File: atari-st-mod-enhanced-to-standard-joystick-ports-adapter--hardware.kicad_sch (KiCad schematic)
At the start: 45 parts, among them J1 Joy0/Mouse, J2 Joy1, J3 OLED 128×64, J4 Enhanced Joystick Port, J5 Joy0/Mouse, J6 Joy1, Q1 1<Vgsth<2, Low Rdson, Vds >10, Q10 1<Vgsth<2, Low Rdson, Vds >10, Q2 1<Vgsth<2, Low Rdson, Vds >10, Q3 1<Vgsth<2, Low Rdson, Vds >10, Q4 1<Vgsth<2, Low Rdson, Vds >10, Q5 1<Vgsth<2, Low Rdson, Vds >10, Q6 1<Vgsth<2, Low Rdson, Vds >10, Q7 1<Vgsth<2, Low Rdson, Vds >10, Q8 1<Vgsth<2, Low Rdson, Vds >10, Q9 1<Vgsth<2, Low Rdson, Vds >10, SW1 Reset, SW2 Selector, SW3 Activate/Change, SW4 Cancel, U1 LM4040DBZ-3

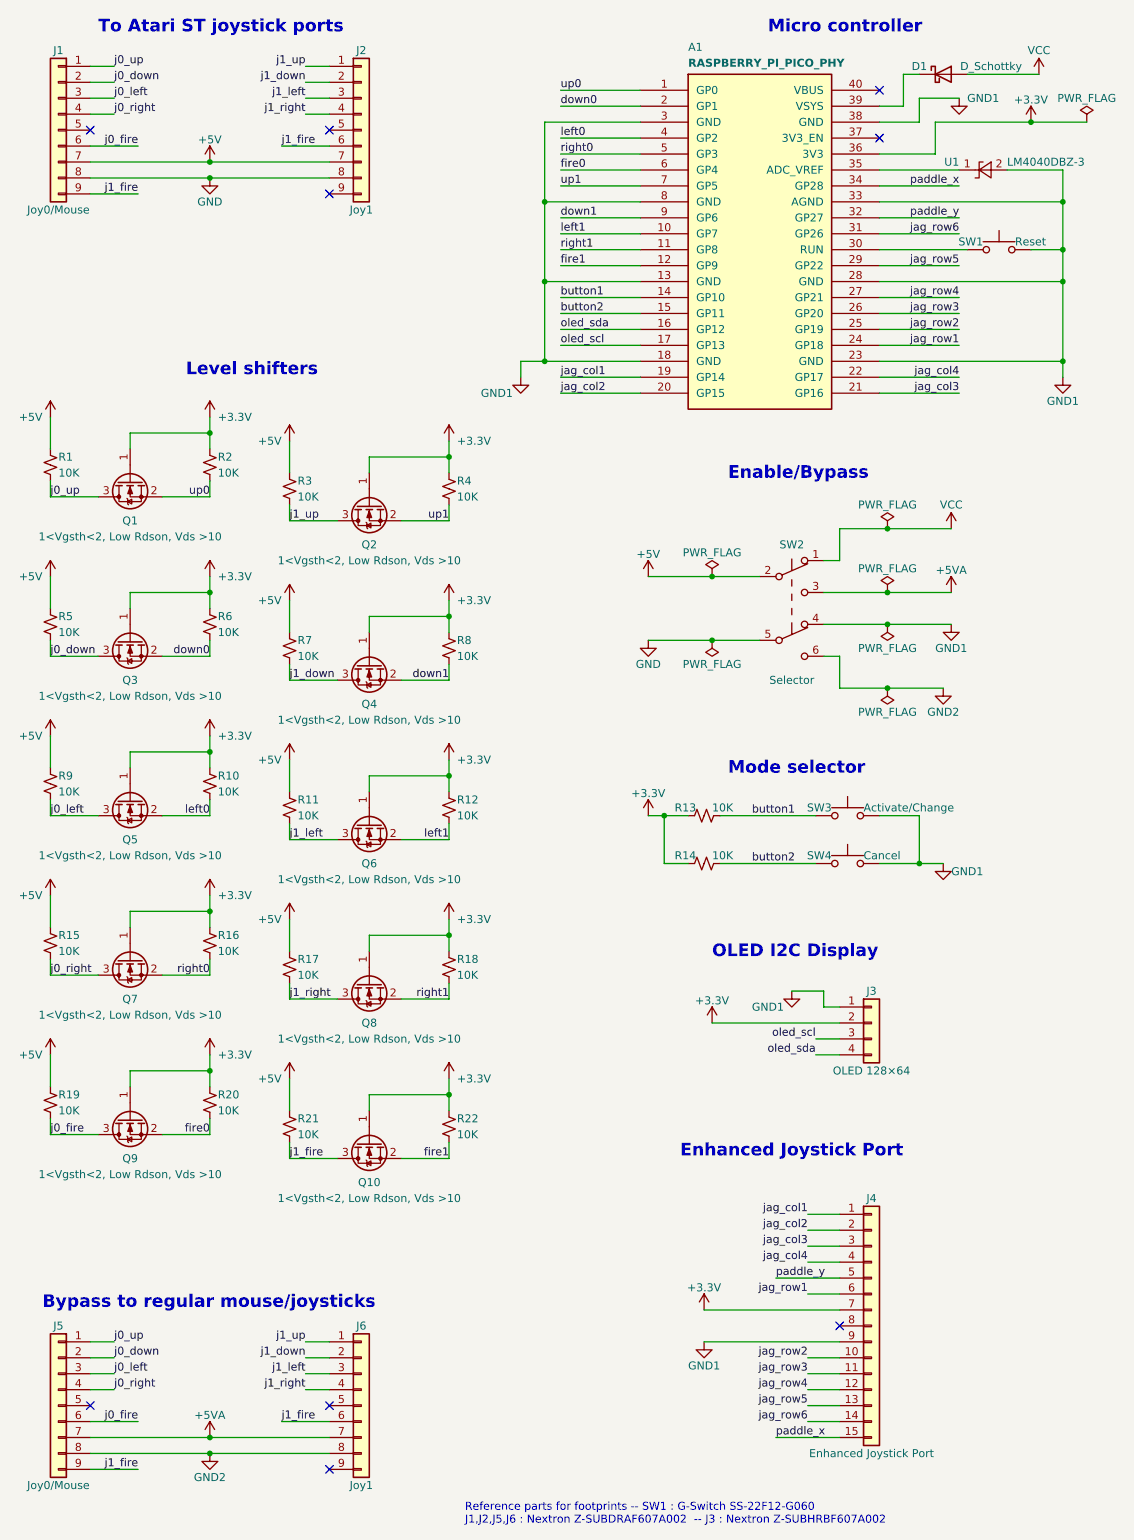
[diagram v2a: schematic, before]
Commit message: rearrange connexion for easier routing
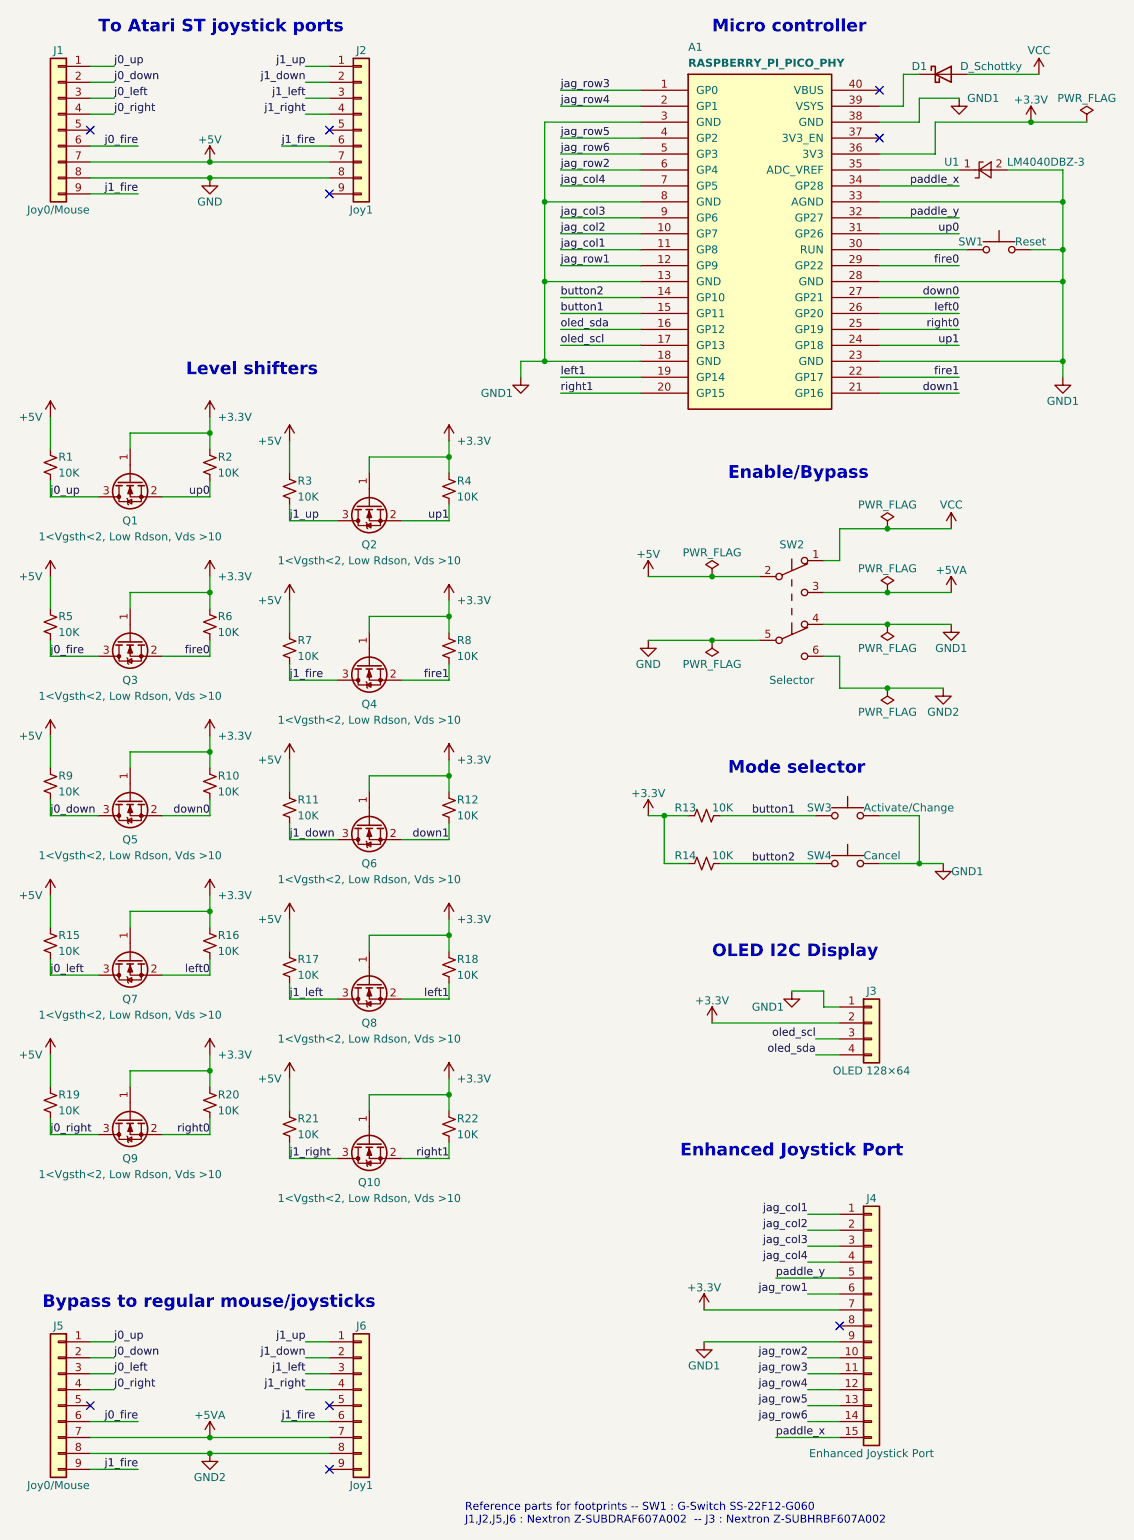
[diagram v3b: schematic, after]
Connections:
- net button1: now also A1.15 (GP11); no longer A1.14 (GP10)
- net button2: now also A1.14 (GP10); no longer A1.15 (GP11)
- net down0: now also A1.27 (GP21), Q5.2 (S), R10.2; no longer A1.2 (GP1), Q3.2 (S), R6.2
- net down1: now also A1.21 (GP16), Q6.2 (S), R12.2; no longer A1.9 (GP6), Q4.2 (S), R8.2
- net fire0: now also A1.29 (GP22), Q3.2 (S), R6.2; no longer A1.6 (GP4), Q9.2 (S), R20.2
- net fire1: now also A1.22 (GP17), Q4.2 (S), R8.2; no longer A1.12 (GP9), Q10.2 (S), R22.2
- net j0_down: now also Q5.3 (D), R9.2; no longer Q3.3 (D), R5.2
- net j0_fire: now also Q3.3 (D), R5.2; no longer Q9.3 (D), R19.2
- net j0_left: now also Q7.3 (D), R15.2; no longer Q5.3 (D), R9.2
- net j0_right: now also Q9.3 (D), R19.2; no longer Q7.3 (D), R15.2
- net j1_down: now also Q6.3 (D), R11.2; no longer Q4.3 (D), R7.2
- net j1_fire: now also Q4.3 (D), R7.2; no longer Q10.3 (D), R21.2
- net j1_left: now also Q8.3 (D), R17.2; no longer Q6.3 (D), R11.2
- net j1_right: now also Q10.3 (D), R21.2; no longer Q8.3 (D), R17.2
- net jag_col1: now also A1.11 (GP8); no longer A1.19 (GP14)
- net jag_col2: now also A1.10 (GP7); no longer A1.20 (GP15)
- net jag_col3: now also A1.9 (GP6); no longer A1.21 (GP16)
- net jag_col4: now also A1.7 (GP5); no longer A1.22 (GP17)
- net jag_row1: now also A1.12 (GP9); no longer A1.24 (GP18)
- net jag_row2: now also A1.6 (GP4); no longer A1.25 (GP19)
- net jag_row3: now also A1.1 (GP0); no longer A1.26 (GP20)
- net jag_row4: now also A1.2 (GP1); no longer A1.27 (GP21)
- net jag_row5: now also A1.4 (GP2); no longer A1.29 (GP22)
- net jag_row6: now also A1.5 (GP3); no longer A1.31 (GP26)
- net left0: now also A1.26 (GP20), Q7.2 (S), R16.2; no longer A1.4 (GP2), Q5.2 (S), R10.2
- net left1: now also A1.19 (GP14), Q8.2 (S), R18.2; no longer A1.10 (GP7), Q6.2 (S), R12.2
- net right0: now also A1.25 (GP19), Q9.2 (S), R20.2; no longer A1.5 (GP3), Q7.2 (S), R16.2
- net right1: now also A1.20 (GP15), Q10.2 (S), R22.2; no longer A1.11 (GP8), Q8.2 (S), R18.2
- net up0: now also A1.31 (GP26); no longer A1.1 (GP0)
- net up1: now also A1.24 (GP18); no longer A1.7 (GP5)
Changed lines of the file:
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@@
     (effects (font (size 2 2) (thickness 0.4) bold) (justify left bottom))
   )
-  (text "Micro controller" (at 139.7 20.32 0)
+  (text "Micro controller" (at 130.81 20.32 0)
     (effects (font (size 2 2) bold) (justify left bottom))
   )
@@
     (effects (font (size 1.27 1.27)) (justify right bottom))
   )
-  (label "up0" (at 106.68 29.21 0)
-    (effects (font (size 1.27 1.27)) (justify left bottom))
-  )
-  (label "jag_row2" (at 170.18 67.31 180)
-    (effects (font (size 1.27 1.27)) (justify right bottom))
-  )
-  (label "fire1" (at 106.68 57.15 0)
-    (effects (font (size 1.27 1.27)) (justify left bottom))
+  (label "up0" (at 170.18 52.07 180)
+    (effects (font (size 1.27 1.27)) (justify right bottom))
+  )
+  (label "jag_row2" (at 106.68 41.91 0)
+    (effects (font (size 1.27 1.27)) (justify left bottom))
+  )
+  (label "fire1" (at 170.18 74.93 180)
+    (effects (font (size 1.27 1.27)) (justify right bottom))
   )
   (label "jag_row3" (at 146.05 233.68 180)
@@
     (effects (font (size 1.27 1.27)) (justify left bottom))
   )
-  (label "jag_row6" (at 170.18 52.07 180)
-    (effects (font (size 1.27 1.27)) (justify right bottom))
+  (label "jag_row6" (at 106.68 39.37 0)
+    (effects (font (size 1.27 1.27)) (justify left bottom))
   )
   (label "oled_sda" (at 106.68 67.31 0)
@@
     (effects (font (size 1.27 1.27)) (justify right bottom))
   )
-  (label "left0" (at 50.8 144.78 180)
+  (label "left0" (at 50.8 170.18 180)
     (effects (font (size 1.27 1.27)) (justify right bottom))
   )
@@
     (effects (font (size 1.27 1.27)) (justify right bottom))
   )
-  (label "button1" (at 106.68 62.23 0)
+  (label "button1" (at 106.68 64.77 0)
     (effects (font (size 1.27 1.27)) (justify left bottom))
   )
@@
     (effects (font (size 1.27 1.27)) (justify right bottom))
   )
-  (label "j0_fire" (at 25.4 195.58 0)
-    (effects (font (size 1.27 1.27)) (justify left bottom))
-  )
-  (label "j1_fire" (at 63.5 199.39 0)
-    (effects (font (size 1.27 1.27)) (justify left bottom))
-  )
-  (label "down0" (at 106.68 31.75 0)
-    (effects (font (size 1.27 1.27)) (justify left bottom))
+  (label "j0_fire" (at 25.4 119.38 0)
+    (effects (font (size 1.27 1.27)) (justify left bottom))
+  )
+  (label "j1_fire" (at 63.5 123.19 0)
+    (effects (font (size 1.27 1.27)) (justify left bottom))
+  )
+  (label "down0" (at 170.18 62.23 180)
+    (effects (font (size 1.27 1.27)) (justify right bottom))
   )
   (label "j0_up" (at 35.56 25.4 0)
     (effects (font (size 1.27 1.27)) (justify left bottom))
   )
-  (label "jag_col2" (at 106.68 77.47 0)
-    (effects (font (size 1.27 1.27)) (justify left bottom))
-  )
-  (label "jag_row5" (at 170.18 57.15 180)
-    (effects (font (size 1.27 1.27)) (justify right bottom))
-  )
-  (label "jag_row1" (at 170.18 69.85 180)
-    (effects (font (size 1.27 1.27)) (justify right bottom))
-  )
-  (label "down1" (at 88.9 123.19 180)
-    (effects (font (size 1.27 1.27)) (justify right bottom))
-  )
-  (label "j0_left" (at 25.4 144.78 0)
-    (effects (font (size 1.27 1.27)) (justify left bottom))
-  )
-  (label "jag_col1" (at 106.68 74.93 0)
+  (label "jag_col2" (at 106.68 52.07 0)
+    (effects (font (size 1.27 1.27)) (justify left bottom))
+  )
+  (label "jag_row5" (at 106.68 36.83 0)
+    (effects (font (size 1.27 1.27)) (justify left bottom))
+  )
+  (label "jag_row1" (at 106.68 57.15 0)
+    (effects (font (size 1.27 1.27)) (justify left bottom))
+  )
+  (label "down1" (at 88.9 148.59 180)
+    (effects (font (size 1.27 1.27)) (justify right bottom))
+  )
+  (label "j0_left" (at 25.4 170.18 0)
+    (effects (font (size 1.27 1.27)) (justify left bottom))
+  )
+  (label "jag_col1" (at 106.68 54.61 0)
     (effects (font (size 1.27 1.27)) (justify left bottom))
   )
@@
     (effects (font (size 1.27 1.27)) (justify right bottom))
   )
-  (label "jag_col3" (at 170.18 77.47 180)
-    (effects (font (size 1.27 1.27)) (justify right bottom))
+  (label "jag_col3" (at 106.68 49.53 0)
+    (effects (font (size 1.27 1.27)) (justify left bottom))
   )
   (label "j0_left" (at 35.56 233.68 0)
     (effects (font (size 1.27 1.27)) (justify left bottom))
   )
-  (label "down1" (at 106.68 49.53 0)
-    (effects (font (size 1.27 1.27)) (justify left bottom))
+  (label "down1" (at 170.18 77.47 180)
+    (effects (font (size 1.27 1.27)) (justify right bottom))
   )
   (label "j0_left" (at 35.56 30.48 0)
@@
     (effects (font (size 1.27 1.27)) (justify right bottom))
   )
-  (label "jag_row3" (at 170.18 64.77 180)
-    (effects (font (size 1.27 1.27)) (justify right bottom))
+  (label "jag_row3" (at 106.68 29.21 0)
+    (effects (font (size 1.27 1.27)) (justify left bottom))
   )
   (label "up1" (at 88.9 97.79 180)
     (effects (font (size 1.27 1.27)) (justify right bottom))
   )
-  (label "jag_col4" (at 170.18 74.93 180)
-    (effects (font (size 1.27 1.27)) (justify right bottom))
-  )
-  (label "right1" (at 106.68 54.61 0)
+  (label "jag_col4" (at 106.68 44.45 0)
+    (effects (font (size 1.27 1.27)) (justify left bottom))
+  )
+  (label "right1" (at 106.68 77.47 0)
     (effects (font (size 1.27 1.27)) (justify left bottom))
   )
@@
     (effects (font (size 1.27 1.27)) (justify right bottom))
   )
-  (label "right1" (at 88.9 173.99 180)
-    (effects (font (size 1.27 1.27)) (justify right bottom))
-  )
-  (label "left1" (at 106.68 52.07 0)
+  (label "right1" (at 88.9 199.39 180)
+    (effects (font (size 1.27 1.27)) (justify right bottom))
+  )
+  (label "left1" (at 106.68 74.93 0)
     (effects (font (size 1.27 1.27)) (justify left bottom))
   )
@@
     (effects (font (size 1.27 1.27)) (justify left bottom))
   )
-  (label "jag_row4" (at 170.18 62.23 180)
-    (effects (font (size 1.27 1.27)) (justify right bottom))
+  (label "jag_row4" (at 106.68 31.75 0)
+    (effects (font (size 1.27 1.27)) (justify left bottom))
   )
   (label "paddle_y" (at 140.97 218.44 0)
@@
     (effects (font (size 1.27 1.27)) (justify right bottom))
   )
-  (label "j1_left" (at 63.5 148.59 0)
-    (effects (font (size 1.27 1.27)) (justify left bottom))
-  )
-  (label "button2" (at 106.68 64.77 0)
-    (effects (font (size 1.27 1.27)) (justify left bottom))
-  )
-  (label "fire1" (at 88.9 199.39 180)
+  (label "j1_left" (at 63.5 173.99 0)
+    (effects (font (size 1.27 1.27)) (justify left bottom))
+  )
+  (label "button2" (at 106.68 62.23 0)
+    (effects (font (size 1.27 1.27)) (justify left bottom))
+  )
+  (label "fire1" (at 88.9 123.19 180)
     (effects (font (size 1.27 1.27)) (justify right bottom))
   )
@@
     (effects (font (size 1.27 1.27)) (justify right bottom))
   )
-  (label "left1" (at 88.9 148.59 180)
+  (label "left1" (at 88.9 173.99 180)
     (effects (font (size 1.27 1.27)) (justify right bottom))
   )
@@
     (effects (font (size 1.27 1.27)) (justify left bottom))
   )
-  (label "fire0" (at 106.68 41.91 0)
-    (effects (font (size 1.27 1.27)) (justify left bottom))
+  (label "fire0" (at 170.18 57.15 180)
+    (effects (font (size 1.27 1.27)) (justify right bottom))
   )
   (label "jag_col1" (at 146.05 208.28 180)
@@
     (effects (font (size 1.27 1.27)) (justify right bottom))
   )
-  (label "left0" (at 106.68 36.83 0)
-    (effects (font (size 1.27 1.27)) (justify left bottom))
+  (label "left0" (at 170.18 64.77 180)
+    (effects (font (size 1.27 1.27)) (justify right bottom))
   )
   (label "j1_fire" (at 62.23 38.1 0)
@@
     (effects (font (size 1.27 1.27)) (justify left bottom))
   )
-  (label "right0" (at 50.8 170.18 180)
-    (effects (font (size 1.27 1.27)) (justify right bottom))
-  )
-  (label "down0" (at 50.8 119.38 180)
+  (label "right0" (at 50.8 195.58 180)
+    (effects (font (size 1.27 1.27)) (justify right bottom))
+  )
+  (label "down0" (at 50.8 144.78 180)
     (effects (font (size 1.27 1.27)) (justify right bottom))
   )
@@
     (effects (font (size 1.27 1.27)) (justify left bottom))
   )
-  (label "j1_right" (at 63.5 173.99 0)
-    (effects (font (size 1.27 1.27)) (justify left bottom))
-  )
-  (label "right0" (at 106.68 39.37 0)
-    (effects (font (size 1.27 1.27)) (justify left bottom))
+  (label "j1_right" (at 63.5 199.39 0)
+    (effects (font (size 1.27 1.27)) (justify left bottom))
+  )
+  (label "right0" (at 170.18 67.31 180)
+    (effects (font (size 1.27 1.27)) (justify right bottom))
   )
   (label "j0_fire" (at 39.37 38.1 180)
     (effects (font (size 1.27 1.27)) (justify right bottom))
   )
-  (label "j0_down" (at 25.4 119.38 0)
+  (label "j0_down" (at 25.4 144.78 0)
     (effects (font (size 1.27 1.27)) (justify left bottom))
   )
@@
     (effects (font (size 1.27 1.27)) (justify right bottom))
   )
-  (label "up1" (at 106.68 44.45 0)
-    (effects (font (size 1.27 1.27)) (justify left bottom))
-  )
-  (label "j0_right" (at 25.4 170.18 0)
+  (label "up1" (at 170.18 69.85 180)
+    (effects (font (size 1.27 1.27)) (justify right bottom))
+  )
+  (label "j0_right" (at 25.4 195.58 0)
     (effects (font (size 1.27 1.27)) (justify left bottom))
   )
@@
     (effects (font (size 1.27 1.27)) (justify right bottom))
   )
-  (label "j1_down" (at 63.5 123.19 0)
+  (label "j1_down" (at 63.5 148.59 0)
     (effects (font (size 1.27 1.27)) (justify left bottom))
   )
@@
     (effects (font (size 1.27 1.27)) (justify right bottom))
   )
-  (label "fire0" (at 50.8 195.58 180)
-    (effects (font (size 1.27 1.27)) (justify right bottom))
-  )
+  (label "fire0" (at 50.8 119.38 180)
+    (effects (font (size 1.27 1.27)) (justify right bottom))
+  )

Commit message: replace basic pin header connector by proper footprint for oled screen
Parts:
- J3: footprint Connector_PinSocket_2.54mm:PinSocket_1x04_P2.54mm_Vertical -> assemblies_displays_oled:oled_display_iic_128x64pix__outer_26.70x19.26mm__inner_21.74x11.2mm
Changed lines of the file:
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@@
     (property "Reference" "J3" (id 0) (at 156.21 172.72 0))
     (property "Value" "OLED 128×64" (id 1) (at 156.21 185.42 0))
-    (property "Footprint" "Connector_PinSocket_2.54mm:PinSocket_1x04_P2.54mm_Vertical" (id 2) (at 156.21 177.8 0)
+    (property "Footprint" "assemblies_displays_oled:oled_display_iic_128x64pix__outer_26.70x19.26mm__inner_21.74x11.2mm" (id 2) (at 156.21 177.8 0)
       (effects (font (size 1.27 1.27)) hide)
     )
@@
     )
     (path "/87beaccd-9491-499a-bd97-523fb030f5ba"
-      (reference "J3") (unit 1) (value "OLED 128×64") (footprint "Connector_PinSocket_2.54mm:PinSocket_1x04_P2.54mm_Vertical")
+      (reference "J3") (unit 1) (value "OLED 128×64") (footprint "assemblies_displays_oled:oled_display_iic_128x64pix__outer_26.70x19.26mm__inner_21.74x11.2mm")
     )
     (path "/413a6d7b-7637-4c53-9629-c2c873aa85eb"
